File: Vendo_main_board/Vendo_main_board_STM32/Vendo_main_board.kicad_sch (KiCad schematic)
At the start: 109 parts, among them J1 Screw_Terminal_01x04, J10 Screw_Terminal_01x03, J11 Screw_Terminal_01x02, J12 Screw_Terminal_01x03, J2 Barrel_Jack_MountingPin, J3 Conn_01x05_Pin, J4 Conn_01x05_Pin, J5 BOOT, J6 Screw_Terminal_01x04, J7 FTDI, J9 Conn_01x04_Pin, Q1 Q_NMOS_Depletion_GSD, Q2 Q_NMOS_Depletion_GSD, Q3 Q_NMOS_Depletion_GSD, Q4 Q_NMOS_Depletion_GSD, SW1 SW_Push, SW2 SW_Push, SW3 SW_Push, SW4 SW_Push, SW5 SW_Slide_DPDT, U1 AMS1117-3.3, U2 TPS54331D, U3 STM32F103C8T6, U4 PC817, Y1 32.768kHz, Y2 8MHz

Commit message: - update pcb
- updated pcb placement
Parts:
- J1, J6: footprint TerminalBlock_MetzConnect:TerminalBlock_MetzConnect_Type101_RT01604HBWC_1x04_P5.08mm_Horizontal -> TerminalBlock:TerminalBlock_Xinya_XY308-2.54-4P_1x04_P2.54mm_Horizontal
- J10: footprint TerminalBlock_MetzConnect:TerminalBlock_MetzConnect_Type101_RT01603HBWC_1x03_P5.08mm_Horizontal -> TerminalBlock:TerminalBlock_Xinya_XY308-2.54-3P_1x03_P2.54mm_Horizontal
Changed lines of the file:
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@@
 			)
 		)
-		(property "Footprint" "TerminalBlock_MetzConnect:TerminalBlock_MetzConnect_Type101_RT01603HBWC_1x03_P5.08mm_Horizontal"
+		(property "Footprint" "TerminalBlock:TerminalBlock_Xinya_XY308-2.54-3P_1x03_P2.54mm_Horizontal"
 			(at 481.3643 117.4685 0)
 			(effects
@@
 			)
 		)
-		(property "Footprint" "TerminalBlock_MetzConnect:TerminalBlock_MetzConnect_Type101_RT01604HBWC_1x04_P5.08mm_Horizontal"
+		(property "Footprint" "TerminalBlock:TerminalBlock_Xinya_XY308-2.54-4P_1x04_P2.54mm_Horizontal"
 			(at 336.9919 288.29 0)
 			(effects
@@
 			)
 		)
-		(property "Footprint" "TerminalBlock_MetzConnect:TerminalBlock_MetzConnect_Type101_RT01604HBWC_1x04_P5.08mm_Horizontal"
+		(property "Footprint" "TerminalBlock:TerminalBlock_Xinya_XY308-2.54-4P_1x04_P2.54mm_Horizontal"
 			(at 253.1719 289.56 0)
 			(effects

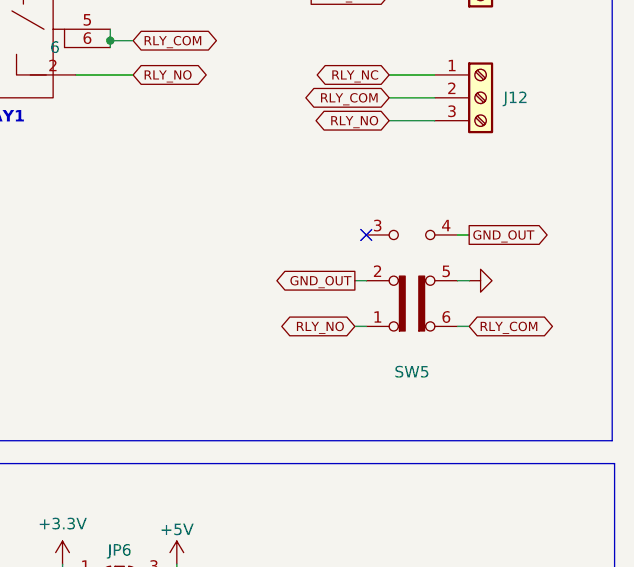
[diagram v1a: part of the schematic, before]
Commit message: -
-update button mode for relay
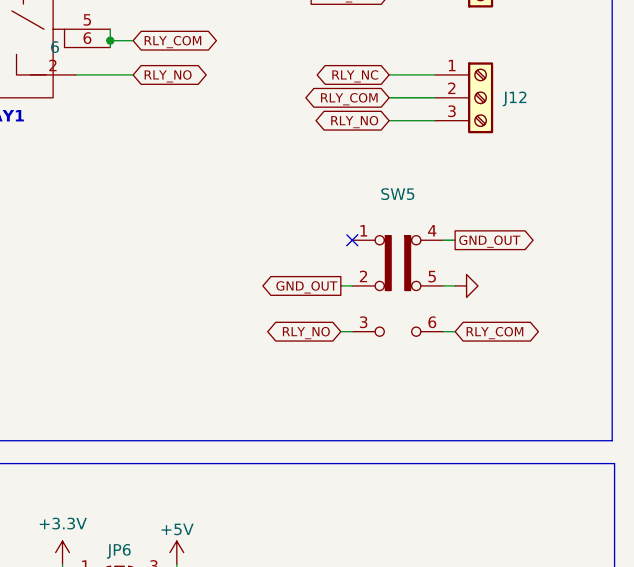
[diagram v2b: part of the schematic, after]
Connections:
- net RLY_NO: now also SW5.3 (C); no longer SW5.1 (A)
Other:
- moved on the sheet: SW5
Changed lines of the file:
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@@
 	)
 	(no_connect
-		(at 553.8057 214.63)
+		(at 552.2475 215.2135)
 	)
 	(no_connect
@@
 	(wire
 		(pts
-			(xy 563.9657 214.63) (xy 565.2357 214.63)
+			(xy 562.4075 215.2135) (xy 563.6775 215.2135)
 		)
 		(stroke
@@
 	(wire
 		(pts
-			(xy 563.9657 224.79) (xy 565.2357 224.79)
+			(xy 562.4075 225.3735) (xy 563.6775 225.3735)
 		)
 		(stroke
@@
 	(wire
 		(pts
-			(xy 552.5357 224.79) (xy 553.8057 224.79)
+			(xy 550.9775 225.3735) (xy 552.2475 225.3735)
 		)
 		(stroke
@@
 	(wire
 		(pts
-			(xy 552.5357 219.71) (xy 553.8057 219.71)
+			(xy 550.9775 220.2935) (xy 552.2475 220.2935)
 		)
 		(stroke
@@
 	(wire
 		(pts
-			(xy 563.9657 219.71) (xy 565.2357 219.71)
+			(xy 562.4075 220.2935) (xy 563.6775 220.2935)
 		)
 		(stroke
@@
 	(global_label "GND_OUT"
 		(shape output)
-		(at 552.5357 219.71 180)
+		(at 550.9775 220.2935 180)
 		(fields_autoplaced yes)
 		(effects
@@
 		)
 		(property "Intersheetrefs" "${INTERSHEET_REFS}"
-			(at 543.3744 219.71 0)
+			(at 541.8162 220.2935 0)
 			(effects
 				(font
@@
 	(global_label "RLY_NO"
 		(shape bidirectional)
-		(at 552.5357 224.79 180)
+		(at 550.9775 225.3735 180)
 		(fields_autoplaced yes)
 		(effects
@@
 		)
 		(property "Intersheetrefs" "${INTERSHEET_REFS}"
-			(at 543.6465 224.79 0)
+			(at 542.0883 225.3735 0)
 			(effects
 				(font
@@
 	(global_label "RLY_COM"
 		(shape bidirectional)
-		(at 565.2357 224.79 0)
+		(at 563.6775 225.3735 0)
 		(fields_autoplaced yes)
 		(effects
@@
 		)
 		(property "Intersheetrefs" "${INTERSHEET_REFS}"
-			(at 575.2376 224.79 0)
+			(at 573.6794 225.3735 0)
 			(effects
 				(font
@@
 	(global_label "GND_OUT"
 		(shape output)
-		(at 565.2357 214.63 0)
+		(at 563.6775 215.2135 0)
 		(fields_autoplaced yes)
 		(effects
@@
 		)
 		(property "Intersheetrefs" "${INTERSHEET_REFS}"
-			(at 574.397 214.63 0)
+			(at 572.8388 215.2135 0)
 			(effects
 				(font
@@
 	(symbol
 		(lib_id "Switch:SW_Slide_DPDT")
-		(at 558.8857 219.71 0)
-		(mirror x)
+		(at 557.3275 220.2935 0)
 		(unit 1)
 		(exclude_from_sim no)
@@
 		(dnp no)
 		(property "Reference" "SW5"
-			(at 558.8857 229.87 0)
+			(at 557.3275 210.1335 0)
 			(effects
 				(font
@@
 		)
 		(property "Value" "SW_Slide_DPDT"
-			(at 558.8857 227.33 0)
+			(at 557.3275 212.6735 0)
 			(effects
 				(font
@@
 		)
 		(property "Footprint" "InnovKits:DPDT_PUSH"
-			(at 572.8557 224.79 0)
+			(at 571.2975 215.2135 0)
 			(effects
 				(font
@@
 		)
 		(property "Datasheet" "~"
-			(at 558.8857 219.71 0)
+			(at 557.3275 220.2935 0)
 			(effects
 				(font
@@
 		)
 		(property "Description" "Slide Switch, dual pole double throw"
-			(at 558.8857 219.71 0)
+			(at 557.3275 220.2935 0)
 			(effects
 				(font
@@
 		)
 		(property "BOX" ""
-			(at 558.8857 219.71 0)
+			(at 557.3275 220.2935 0)
 			(effects
 				(font
@@
 		)
 		(property "Delivery Status" ""
-			(at 558.8857 219.71 0)
+			(at 557.3275 220.2935 0)
 			(effects
 				(font
@@
 		)
 		(property "Manufacturer_Name" ""
-			(at 558.8857 219.71 0)
+			(at 557.3275 220.2935 0)
 			(effects
 				(font
@@
 		)
 		(property "Manufacturer_Part_Number" ""
-			(at 558.8857 219.71 0)
+			(at 557.3275 220.2935 0)
 			(effects
 				(font
@@
 		)
 		(property "Order  Status" ""
-			(at 558.8857 219.71 0)
+			(at 557.3275 220.2935 0)
 			(effects
 				(font
@@
 		)
 		(property "Order Link" ""
-			(at 558.8857 219.71 0)
+			(at 557.3275 220.2935 0)
 			(effects
 				(font
@@
 		)
 		(property "Parts Needed" ""
-			(at 558.8857 219.71 0)
+			(at 557.3275 220.2935 0)
 			(effects
 				(font
@@
 		)
 		(property "QTY.STOCK-ONHAND" ""
-			(at 558.8857 219.71 0)
+			(at 557.3275 220.2935 0)
 			(effects
 				(font
@@
 		)
 		(property "Sim.Type" ""
-			(at 558.8857 219.71 0)
+			(at 557.3275 220.2935 0)
 			(effects
 				(font
@@
 		(lib_name "GND_1")
 		(lib_id "power:GND")
-		(at 565.2357 219.71 90)
-		(mirror x)
+		(at 563.6775 220.2935 90)
 		(unit 1)
 		(exclude_from_sim no)
@@
 		(dnp no)
 		(property "Reference" "#PWR078"
-			(at 571.5857 219.71 0)
+			(at 570.0275 220.2935 0)
 			(effects
 				(font
@@
 		)
 		(property "Value" "GND"
-			(at 570.3157 219.71 0)
+			(at 568.7575 220.2935 0)
 			(effects
 				(font
@@
 		)
 		(property "Footprint" ""
-			(at 565.2357 219.71 0)
+			(at 563.6775 220.2935 0)
 			(effects
 				(font
@@
 		)
 		(property "Datasheet" ""
-			(at 565.2357 219.71 0)
+			(at 563.6775 220.2935 0)
 			(effects
 				(font
@@
 		)
 		(property "Description" "Power symbol creates a global label with name \"GND\" , ground"
-			(at 565.2357 219.71 0)
+			(at 563.6775 220.2935 0)
 			(effects
 				(font

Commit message: stm32 and esp32 version edit
stm32 ver solid gnd plane to buck conv, adjust buttons to smd , btn1 to 3 and reset
esp32 version adjust slave conn by 1mm far away on the sma hole, adjust button 1 ,2 and reset.
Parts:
- SW1, SW2, SW3, SW4: footprint Button_Switch_THT:SW_PUSH_6mm_H5mm -> Button_Switch_SMD:SW_SPST_PTS645
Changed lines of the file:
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@@
 			)
 		)
-		(property "Footprint" "Button_Switch_THT:SW_PUSH_6mm_H5mm"
+		(property "Footprint" "Button_Switch_SMD:SW_SPST_PTS645"
 			(at 344.6119 232.41 0)
 			(effects
@@
 			)
 		)
-		(property "Footprint" "Button_Switch_THT:SW_PUSH_6mm_H5mm"
+		(property "Footprint" "Button_Switch_SMD:SW_SPST_PTS645"
 			(at 405.5719 299.72 0)
 			(effects
@@
 			)
 		)
-		(property "Footprint" "Button_Switch_THT:SW_PUSH_6mm_H5mm"
+		(property "Footprint" "Button_Switch_SMD:SW_SPST_PTS645"
 			(at 375.0919 299.72 0)
 			(effects
@@
 			)
 		)
-		(property "Footprint" "Button_Switch_THT:SW_PUSH_6mm_H5mm"
+		(property "Footprint" "Button_Switch_SMD:SW_SPST_PTS645"
 			(at 434.7819 299.72 0)
 			(effects
